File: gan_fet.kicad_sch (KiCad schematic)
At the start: 7 parts, among them J1 Conn_01x04_Male, Q1 EPC2036, U1 NPC81074

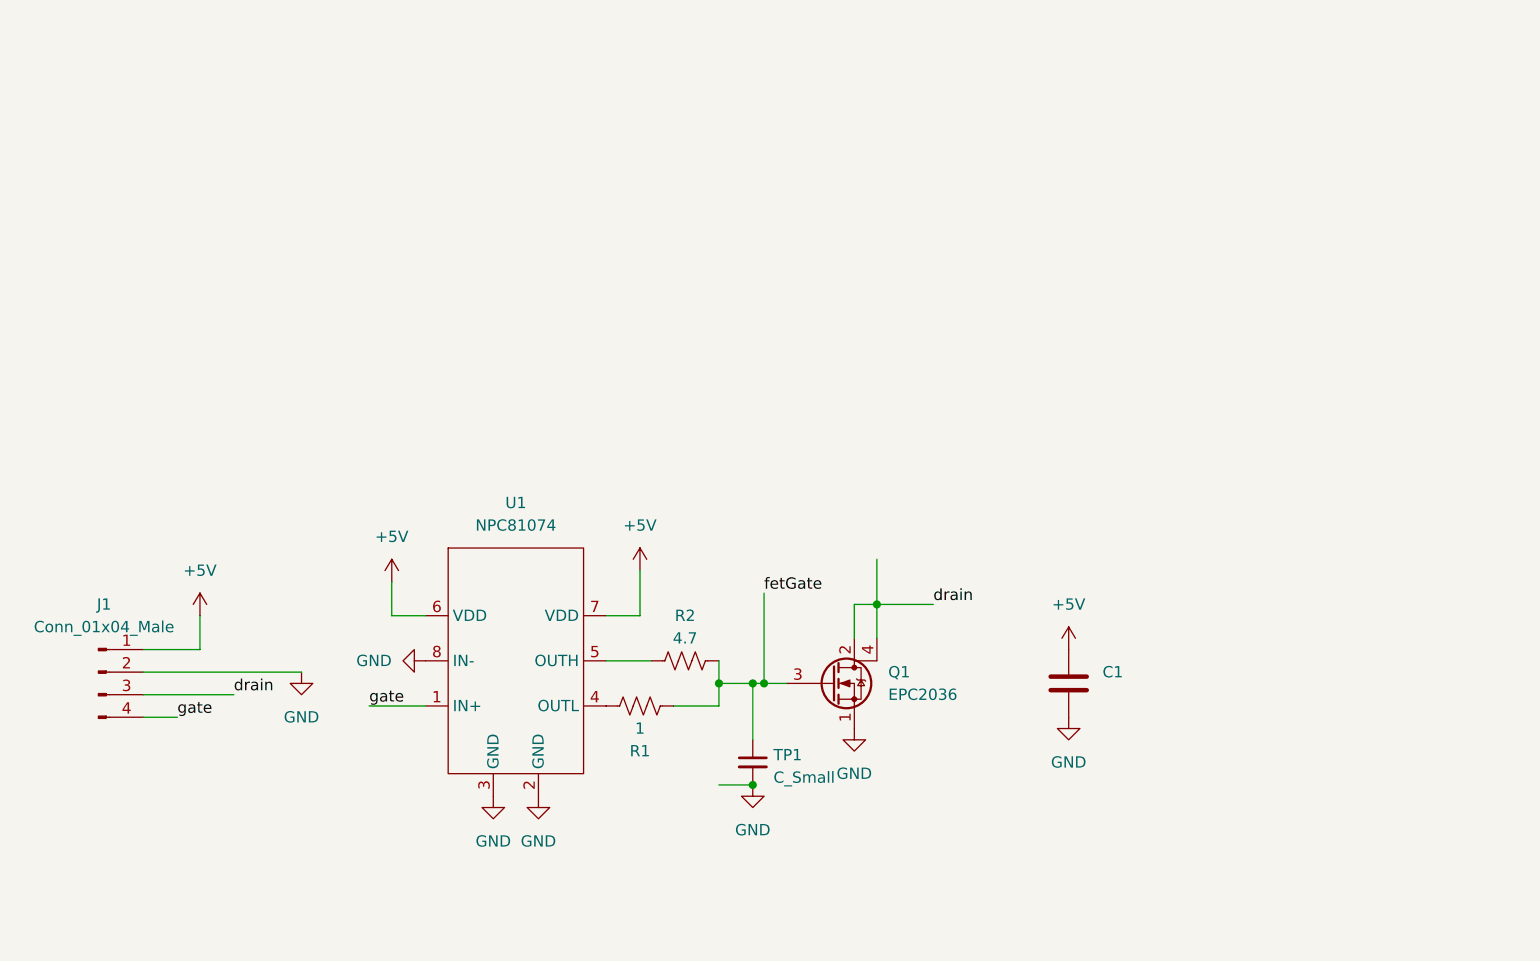
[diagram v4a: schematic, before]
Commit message: Downsized board and replaced driver
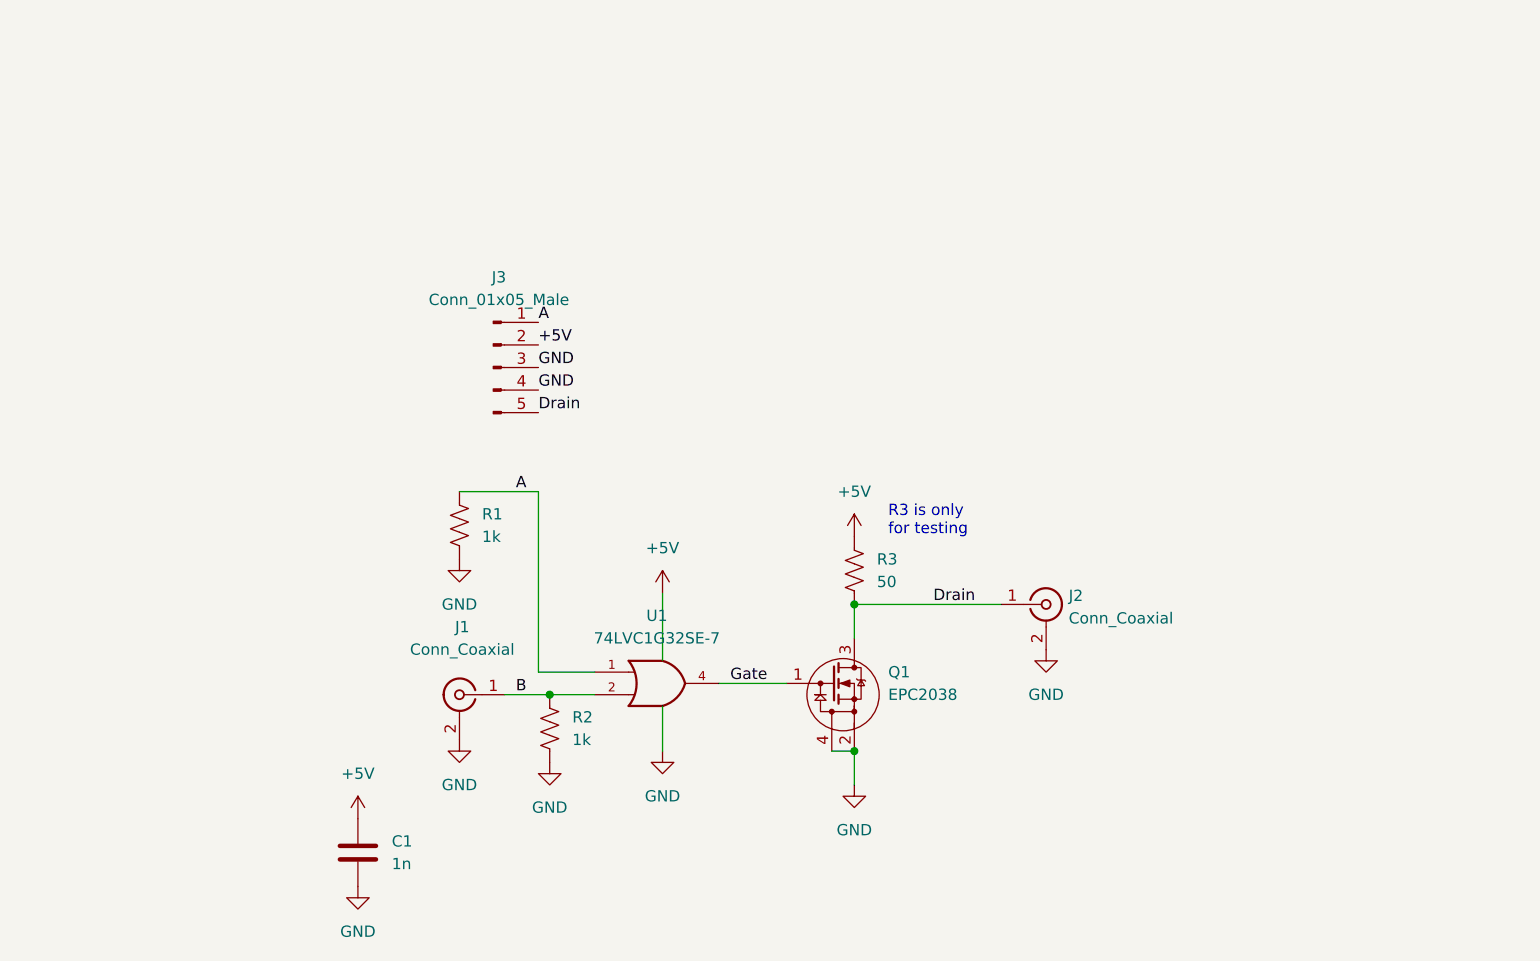
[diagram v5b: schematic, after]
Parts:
- removed J1: Conn_01x04_Male, Connector_PinHeader_2.54mm:PinHeader_1x04_P2.54mm_Horizontal, symbol Connector:Conn_01x04_Male
- removed TP1: C_Small, Resistor_SMD:R_1206_3216Metric, symbol Device:C_Small
- removed U1: NPC81074, Package_SO:SOIC-8_3.9x4.9mm_P1.27mm, symbol gan_fet:NPC81074
- added J1, J2: Conn_Coaxial, Connector_Coaxial:SMA_Amphenol_132289_EdgeMount, symbol Connector:Conn_Coaxial
- added J3: Conn_01x05_Male, Connector_PinHeader_2.54mm:PinHeader_1x05_P2.54mm_Vertical, symbol Connector:Conn_01x05_Male
- added R3: 50, Resistor_SMD:R_0603_1608Metric, symbol Device:R_US
- added U1: 74LVC1G32SE-7, Package_TO_SOT_SMD:SOT-353_SC-70-5, symbol 74xGxx:74LVC1G32
- C1: value (none) -> 1n; footprint (none) -> Capacitor_SMD:C_0603_1608Metric
- Q1: value EPC2036 -> EPC2038; symbol Device:Q_NMOS_SDGD -> gan_fet:EPC2038
- R1: value 1 -> 1k; footprint Resistor_SMD:R_0805_2012Metric_Pad1.20x1.40mm_HandSolder -> Resistor_SMD:R_0603_1608Metric
- R2: value 4.7 -> 1k; footprint Resistor_SMD:R_0805_2012Metric_Pad1.20x1.40mm_HandSolder -> Resistor_SMD:R_0603_1608Metric
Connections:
- net drain is gone; now on net GND: Q1.2 (S), Q1.4 (S)
- net +5V: now also J3.2 (Pin_2), R3.1, U1.5 (VCC)
- net GND: now also R1.2, R2.2, J1.2 (Ext), J2.2 (Ext), J3.3 (Pin_3), J3.4 (Pin_4), U1.3 (GND); no longer Q1.1 (S)
- net A: now reaches R1.1
- net A: now also J3.1 (Pin_1), U1.1
- net B: now reaches R2.1
- net B: now also J1.1 (In), U1.2
- removed net fetGate: Q1.3 (G), R1.2, R2.2
- new net Drain: J2.1 (In), J3.5 (Pin_5), Q1.3 (D), R3.2
- new net Gate: Q1.1 (G), U1.4
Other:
- note added: "R3 is only for testing"
- moved on the sheet: C1

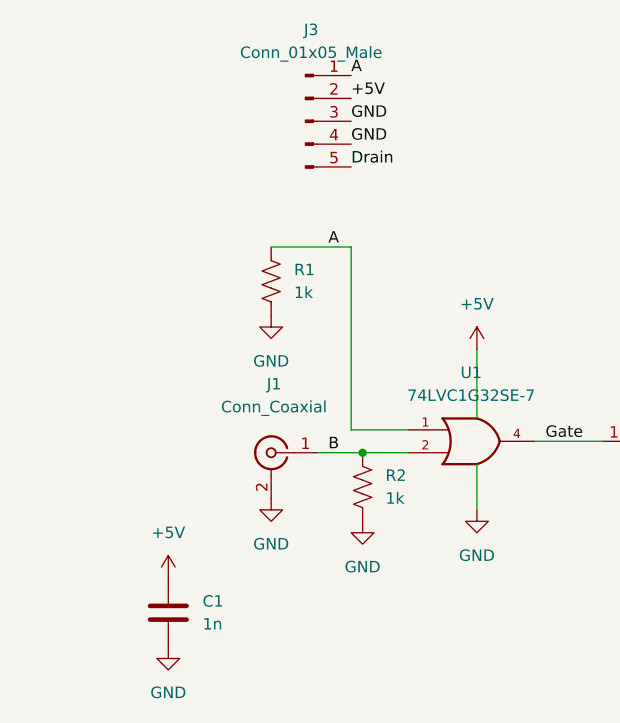
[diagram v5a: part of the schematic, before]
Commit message: Downsized to reduce gate inductance
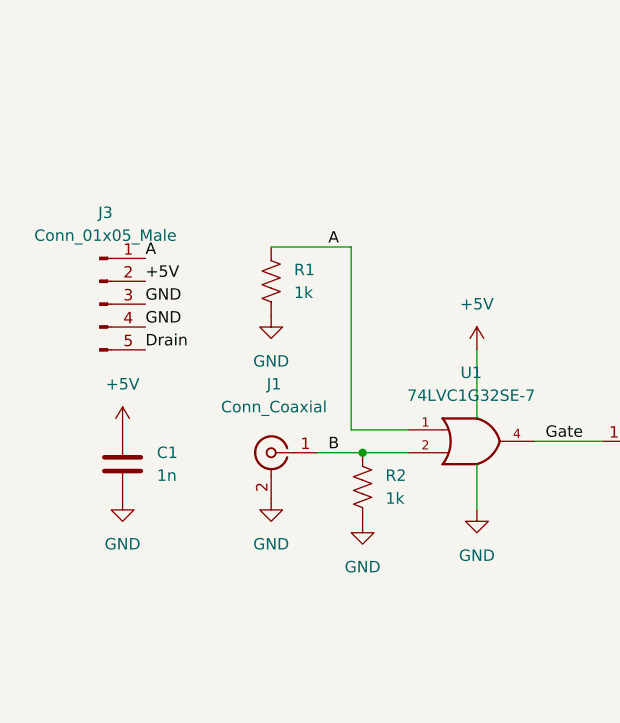
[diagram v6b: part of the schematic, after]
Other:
- moved on the sheet: C1, J3
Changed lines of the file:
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@@
     (effects (font (size 1.27 1.27)) (justify left bottom))
   )
-  (label "+5V" (at 100.33 52.07 0)
-    (effects (font (size 1.27 1.27)) (justify left bottom))
-  )
-  (label "A" (at 100.33 49.53 0)
-    (effects (font (size 1.27 1.27)) (justify left bottom))
-  )
-  (label "Drain" (at 100.33 59.69 0)
-    (effects (font (size 1.27 1.27)) (justify left bottom))
-  )
-  (label "GND" (at 100.33 57.15 0)
+  (label "+5V" (at 77.47 72.39 0)
+    (effects (font (size 1.27 1.27)) (justify left bottom))
+  )
+  (label "A" (at 77.47 69.85 0)
+    (effects (font (size 1.27 1.27)) (justify left bottom))
+  )
+  (label "Drain" (at 77.47 80.01 0)
+    (effects (font (size 1.27 1.27)) (justify left bottom))
+  )
+  (label "GND" (at 77.47 77.47 0)
     (effects (font (size 1.27 1.27)) (justify left bottom))
   )
@@
     (effects (font (size 1.27 1.27)) (justify left bottom))
   )
-  (label "GND" (at 100.33 54.61 0)
+  (label "GND" (at 77.47 74.93 0)
     (effects (font (size 1.27 1.27)) (justify left bottom))
   )
@@
     (pin "2")
   )
-  (symbol (lib_id "Connector:Conn_01x05_Male") (at 95.25 54.61 0) (unit 1)
-    (in_bom yes) (on_board yes) (fields_autoplaced)
-    (property "Reference" "J3" (id 0) (at 95.885 44.45 0))
-    (property "Value" "Conn_01x05_Male" (id 1) (at 95.885 46.99 0))
-    (property "Footprint" "Connector_PinHeader_2.54mm:PinHeader_1x05_P2.54mm_Vertical" (id 2) (at 95.25 54.61 0)
-      (effects (font (size 1.27 1.27)) hide)
-    )
-    (property "Datasheet" "~" (id 3) (at 95.25 54.61 0)
+  (symbol (lib_id "Connector:Conn_01x05_Male") (at 72.39 74.93 0) (unit 1)
+    (in_bom yes) (on_board yes) (fields_autoplaced)
+    (property "Reference" "J3" (id 0) (at 73.025 64.77 0))
+    (property "Value" "Conn_01x05_Male" (id 1) (at 73.025 67.31 0))
+    (property "Footprint" "Connector_PinHeader_2.54mm:PinHeader_1x05_P2.54mm_Vertical" (id 2) (at 72.39 74.93 0)
+      (effects (font (size 1.27 1.27)) hide)
+    )
+    (property "Datasheet" "~" (id 3) (at 72.39 74.93 0)
       (effects (font (size 1.27 1.27)) hide)
     )
@@
     (pin "1")
   )
-  (symbol (lib_id "Device:C") (at 80.01 109.22 0) (unit 1)
-    (in_bom yes) (on_board yes) (fields_autoplaced)
-    (property "Reference" "C1" (id 0) (at 83.82 107.9499 0)
-      (effects (font (size 1.27 1.27)) (justify left))
-    )
-    (property "Value" "1n" (id 1) (at 83.82 110.4899 0)
-      (effects (font (size 1.27 1.27)) (justify left))
-    )
-    (property "Footprint" "Capacitor_SMD:C_0603_1608Metric" (id 2) (at 80.9752 113.03 0)
-      (effects (font (size 1.27 1.27)) hide)
-    )
-    (property "Datasheet" "~" (id 3) (at 80.01 109.22 0)
-      (effects (font (size 1.27 1.27)) hide)
-    )
-    (pin "1")
-    (pin "2")
-  )
-  (symbol (lib_id "power:+5V") (at 80.01 105.41 0) (unit 1)
-    (in_bom yes) (on_board yes) (fields_autoplaced)
-    (property "Reference" "#PWR09" (id 0) (at 80.01 109.22 0)
-      (effects (font (size 1.27 1.27)) hide)
-    )
-    (property "Value" "+5V" (id 1) (at 80.01 100.33 0))
-    (property "Footprint" "" (id 2) (at 80.01 105.41 0)
-      (effects (font (size 1.27 1.27)) hide)
-    )
-    (property "Datasheet" "" (id 3) (at 80.01 105.41 0)
+  (symbol (lib_id "Device:C") (at 74.93 92.71 0) (unit 1)
+    (in_bom yes) (on_board yes) (fields_autoplaced)
+    (property "Reference" "C1" (id 0) (at 78.74 91.4399 0)
+      (effects (font (size 1.27 1.27)) (justify left))
+    )
+    (property "Value" "1n" (id 1) (at 78.74 93.9799 0)
+      (effects (font (size 1.27 1.27)) (justify left))
+    )
+    (property "Footprint" "Capacitor_SMD:C_0603_1608Metric" (id 2) (at 75.8952 96.52 0)
+      (effects (font (size 1.27 1.27)) hide)
+    )
+    (property "Datasheet" "~" (id 3) (at 74.93 92.71 0)
+      (effects (font (size 1.27 1.27)) hide)
+    )
+    (pin "1")
+    (pin "2")
+  )
+  (symbol (lib_id "power:+5V") (at 74.93 88.9 0) (unit 1)
+    (in_bom yes) (on_board yes) (fields_autoplaced)
+    (property "Reference" "#PWR09" (id 0) (at 74.93 92.71 0)
+      (effects (font (size 1.27 1.27)) hide)
+    )
+    (property "Value" "+5V" (id 1) (at 74.93 83.82 0))
+    (property "Footprint" "" (id 2) (at 74.93 88.9 0)
+      (effects (font (size 1.27 1.27)) hide)
+    )
+    (property "Datasheet" "" (id 3) (at 74.93 88.9 0)
       (effects (font (size 1.27 1.27)) hide)
     )
@@
     (pin "2")
   )
-  (symbol (lib_id "power:GND") (at 80.01 113.03 0) (unit 1)
-    (in_bom yes) (on_board yes) (fields_autoplaced)
-    (property "Reference" "#PWR010" (id 0) (at 80.01 119.38 0)
-      (effects (font (size 1.27 1.27)) hide)
-    )
-    (property "Value" "GND" (id 1) (at 80.01 118.11 0))
-    (property "Footprint" "" (id 2) (at 80.01 113.03 0)
-      (effects (font (size 1.27 1.27)) hide)
-    )
-    (property "Datasheet" "" (id 3) (at 80.01 113.03 0)
-      (effects (font (size 1.27 1.27)) hide)
-    )
+  (symbol (lib_id "power:GND") (at 74.93 96.52 0) (unit 1)
+    (in_bom yes) (on_board yes) (fields_autoplaced)
+    (property "Reference" "#PWR010" (id 0) (at 74.93 102.87 0)
+      (effects (font (size 1.27 1.27)) hide)
+    )
+    (property "Value" "GND" (id 1) (at 74.93 101.6 0))
+    (property "Footprint" "" (id 2) (at 74.93 96.52 0)
+      (effects (font (size 1.27 1.27)) hide)
+    )
+    (property "Datasheet" "" (id 3) (at 74.93 96.52 0)
+      (effects (font (size 1.27 1.27)) hide)
+    )

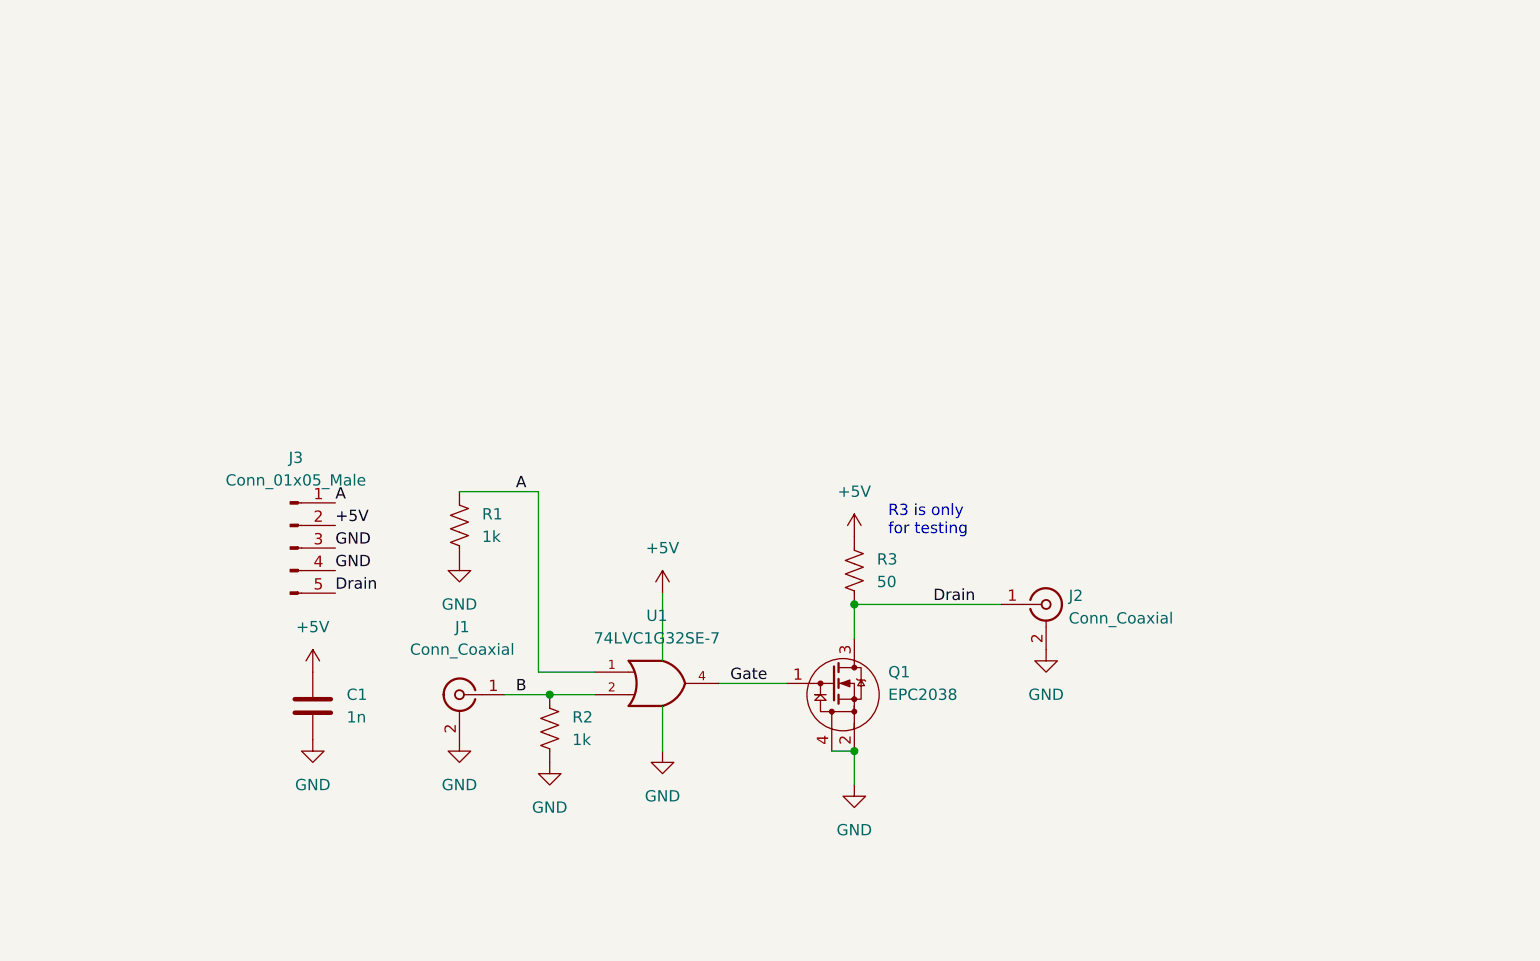
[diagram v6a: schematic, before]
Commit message: Added header for standard filter board
Moved R3 to tie to 12V instead of 5V
Swapped inputs on OR gate
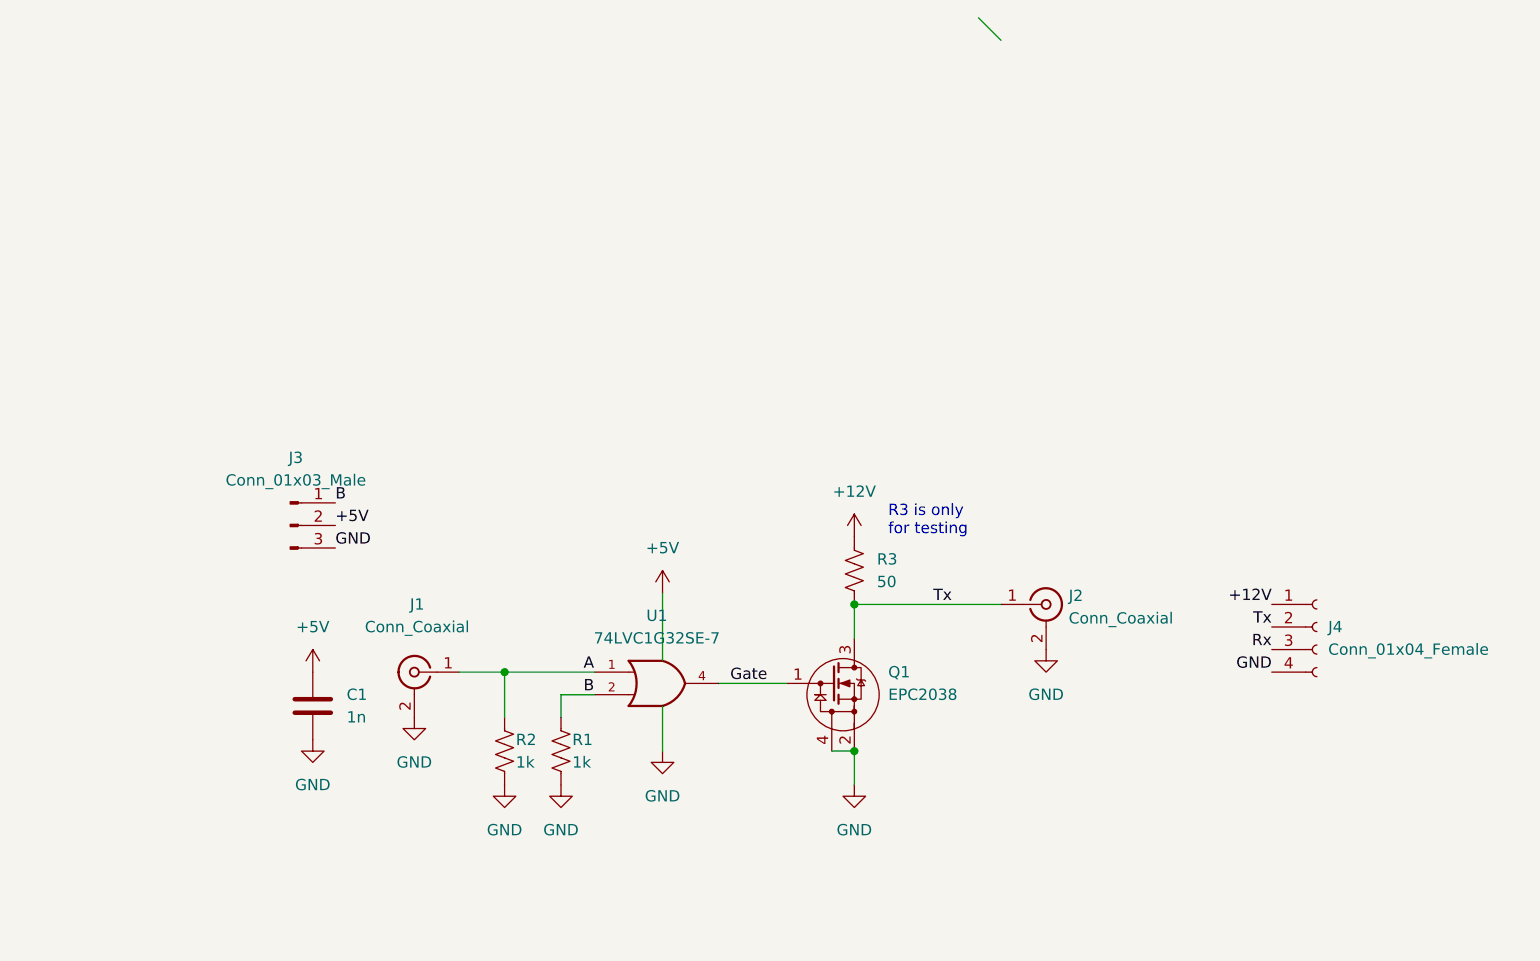
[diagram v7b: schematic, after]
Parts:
- removed J3: Conn_01x05_Male, Connector_PinHeader_2.54mm:PinHeader_1x05_P2.54mm_Vertical, symbol Connector:Conn_01x05_Male
- added J3: Conn_01x03_Male, Connector_PinHeader_2.54mm:PinHeader_1x03_P2.54mm_Vertical, symbol Connector:Conn_01x03_Male
- added J4: Conn_01x04_Female, Connector_PinSocket_2.54mm:PinSocket_1x04_P2.54mm_Vertical, symbol Connector:Conn_01x04_Female
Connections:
- net +5V: now also J3.2 (Pin_2); no longer R3.1
- net A: now also J1.1 (In), R2.1; no longer R1.1
- net B: now also R1.1, J3.1 (Pin_1); no longer J1.1 (In), R2.1
- net GND: now also J3.3 (Pin_3), J4.4 (Pin_4)
- net Drain renamed Tx
- net Tx: now also J4.2 (Pin_2)
- new net +12V: J4.1 (Pin_1), R3.1
- new net Rx: J4.3 (Pin_3)
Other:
- moved on the sheet: J1, R1, R2
